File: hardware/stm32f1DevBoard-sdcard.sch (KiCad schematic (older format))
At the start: 2 parts, among them J3 SDCARD

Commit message: using kicadcloud files
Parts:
- C17: symbol CSMALL -> CPsmall
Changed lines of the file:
@@
-EESchema Schematic File Version 2  date Wed 19 Dec 2012 11:05:56 PM EST
-LIBS:stm32f1DevBoard
+EESchema Schematic File Version 2  date Wed 02 Jan 2013 12:15:05 PM EST
+LIBS:userFavorites
 LIBS:power
-LIBS:device
-LIBS:transistors
-LIBS:conn
-LIBS:linear
-LIBS:regul
-LIBS:74xx
-LIBS:cmos4000
-LIBS:adc-dac
-LIBS:memory
-LIBS:xilinx
-LIBS:special
-LIBS:microcontrollers
-LIBS:dsp
-LIBS:microchip
-LIBS:analog_switches
-LIBS:motorola
-LIBS:texas
-LIBS:intel
-LIBS:audio
-LIBS:interface
-LIBS:digital-audio
-LIBS:philips
-LIBS:display
-LIBS:cypress
-LIBS:siliconi
-LIBS:opto
-LIBS:atmel
-LIBS:contrib
-LIBS:valves
-LIBS:stm32f1DevBoard-cache
 EELAYER 27 0
 EELAYER END
@@
 	5600 3400 5100 3400
 $Comp
-L CSMALL C17
+L CPsmall C17
 U 1 1 50CE3324
 P 7750 4600

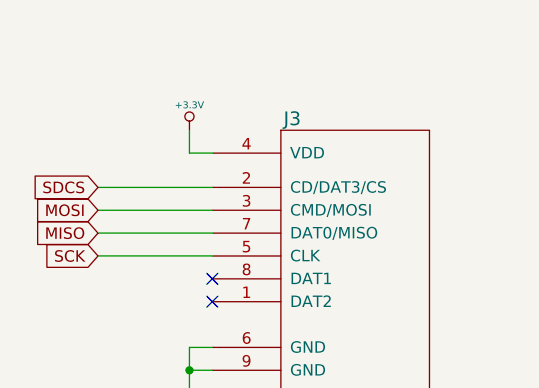
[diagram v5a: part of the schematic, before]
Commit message: added pull resistor on sdcard cs
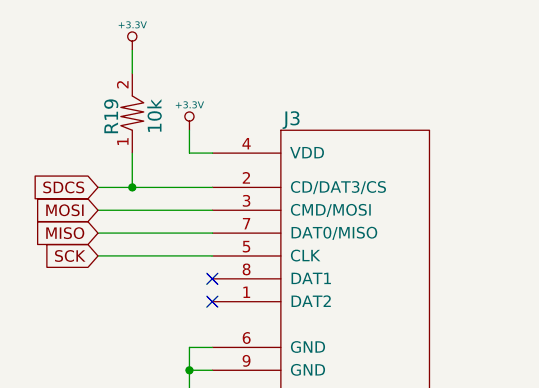
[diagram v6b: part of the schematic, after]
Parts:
- added R19: 10k, symbol R
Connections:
- net +3.3V: now also R19.2
- net SDCS: now also R19.1
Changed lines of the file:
@@
-EESchema Schematic File Version 2  date Wed 02 Jan 2013 12:15:05 PM EST
+EESchema Schematic File Version 2  date Thu 17 Jan 2013 09:41:47 PM EST
 LIBS:userFavorites
 LIBS:power
@@
 Sheet 4 4
 Title ""
-Date "20 dec 2012"
+Date "18 jan 2013"
 Rev ""
 Comp ""
@@
 $EndComp
 $Comp
-L +3.3V #PWR057
+L +3.3V #PWR58
 U 1 1 50CE3309
 P 5500 3150
-F 0 "#PWR057" H 5500 3110 30  0001 C CNN
+F 0 "#PWR58" H 5500 3110 30  0001 C CNN
 F 1 "+3.3V" H 5500 3260 30  0000 C CNN
 	1    5500 3150
@@
 $EndComp
 $Comp
-L GND #PWR058
+L GND #PWR59
 U 1 1 50CE330F
 P 5500 4300
-F 0 "#PWR058" H 5500 4300 30  0001 C CNN
+F 0 "#PWR59" H 5500 4300 30  0001 C CNN
 F 1 "GND" H 5500 4230 30  0001 C CNN
 	1    5500 4300
@@
 $EndComp
 $Comp
-L +3.3V #PWR059
+L +3.3V #PWR60
 U 1 1 50CE332A
 P 7750 4400
-F 0 "#PWR059" H 7750 4360 30  0001 C CNN
+F 0 "#PWR60" H 7750 4360 30  0001 C CNN
 F 1 "+3.3V" H 7750 4510 30  0000 C CNN
 	1    7750 4400
@@
 $EndComp
 $Comp
-L GND #PWR060
+L GND #PWR61
 U 1 1 50CE3330
 P 7750 4800
-F 0 "#PWR060" H 7750 4800 30  0001 C CNN
+F 0 "#PWR61" H 7750 4800 30  0001 C CNN
 F 1 "GND" H 7750 4730 30  0001 C CNN
 	1    7750 4800
@@
 NoConn ~ 5600 3800
 NoConn ~ 5600 3900
+$Comp
+L R R19
+U 1 1 50F8B9A0
+P 5250 3100
+F 0 "R19" H 5260 3190 60  0000 C CNN
+F 1 "10k" H 5260 3000 60  0000 C CNN
+	1    5250 3100
+	0    -1   -1   0
+$EndComp
+$Comp
+L +3.3V #PWR57
+U 1 1 50F8B9B2
+P 5250 2800
+F 0 "#PWR57" H 5250 2760 30  0001 C CNN
+F 1 "+3.3V" H 5250 2910 30  0000 C CNN
+	1    5250 2800
+	1    0    0    -1
+$EndComp
+Wire Wire Line
+	5250 2800 5250 2900
+Wire Wire Line
+	5250 3250 5250 3400
+Connection ~ 5250 3400
 $EndSCHEMATC

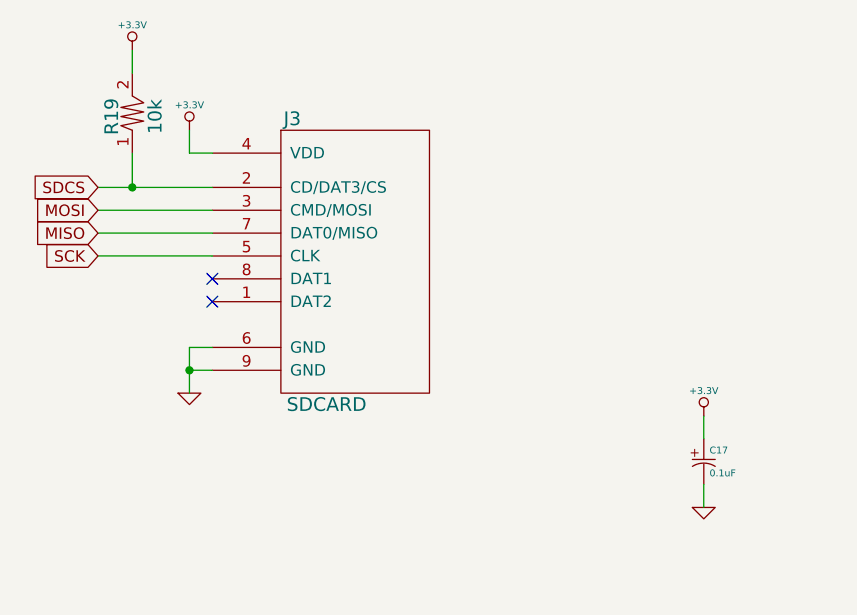
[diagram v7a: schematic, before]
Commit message: fix sdcard
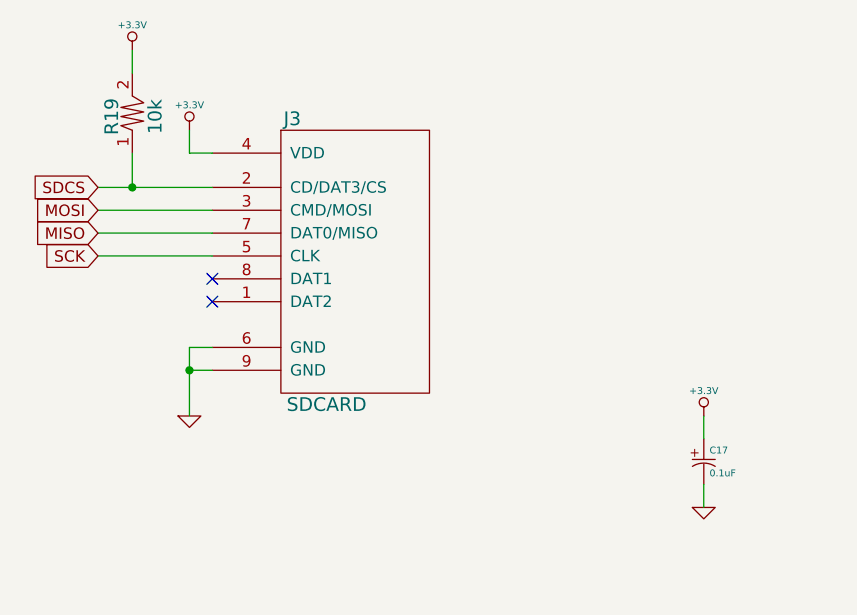
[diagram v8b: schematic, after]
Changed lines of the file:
@@
-EESchema Schematic File Version 2  date Mon 21 Jan 2013 10:28:50 PM EST
+EESchema Schematic File Version 2  date Tue 29 Jan 2013 12:07:46 AM EST
 LIBS:userFavorites
 LIBS:power
@@
 Sheet 4 4
 Title ""
-Date "22 jan 2013"
+Date "29 jan 2013"
 Rev ""
 Comp ""
@@
 $EndComp
 $Comp
-L +3.3V #PWR58
+L +3.3V #PWR057
 U 1 1 50CE3309
 P 5500 3150
-F 0 "#PWR58" H 5500 3110 30  0001 C CNN
+F 0 "#PWR057" H 5500 3110 30  0001 C CNN
 F 1 "+3.3V" H 5500 3260 30  0000 C CNN
 	1    5500 3150
@@
 $EndComp
 $Comp
-L GND #PWR59
+L GND #PWR058
 U 1 1 50CE330F
-P 5500 4300
-F 0 "#PWR59" H 5500 4300 30  0001 C CNN
-F 1 "GND" H 5500 4230 30  0001 C CNN
-	1    5500 4300
+P 5500 4400
+F 0 "#PWR058" H 5500 4400 30  0001 C CNN
+F 1 "GND" H 5500 4330 30  0001 C CNN
+	1    5500 4400
 	1    0    0    -1
 $EndComp
@@
 	5600 4100 5500 4100
 Wire Wire Line
-	5500 4100 5500 4300
+	5500 4100 5500 4400
 Wire Wire Line
 	5600 4200 5500 4200
@@
 	5600 3500 5100 3500
 Wire Wire Line
-	5600 3400 5100 3400
+	5100 3400 5600 3400
 $Comp
 L CPsmall C17
@@
 $EndComp
 $Comp
-L +3.3V #PWR60
+L +3.3V #PWR059
 U 1 1 50CE332A
 P 7750 4400
-F 0 "#PWR60" H 7750 4360 30  0001 C CNN
+F 0 "#PWR059" H 7750 4360 30  0001 C CNN
 F 1 "+3.3V" H 7750 4510 30  0000 C CNN
 	1    7750 4400
@@
 $EndComp
 $Comp
-L GND #PWR61
+L GND #PWR060
 U 1 1 50CE3330
 P 7750 4800
-F 0 "#PWR61" H 7750 4800 30  0001 C CNN
+F 0 "#PWR060" H 7750 4800 30  0001 C CNN
 F 1 "GND" H 7750 4730 30  0001 C CNN
 	1    7750 4800
@@
 $EndComp
 $Comp
-L +3.3V #PWR57
+L +3.3V #PWR061
 U 1 1 50F8B9B2
 P 5250 2800
-F 0 "#PWR57" H 5250 2760 30  0001 C CNN
+F 0 "#PWR061" H 5250 2760 30  0001 C CNN
 F 1 "+3.3V" H 5250 2910 30  0000 C CNN
 	1    5250 2800
